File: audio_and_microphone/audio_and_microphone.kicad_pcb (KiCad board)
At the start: 2 copper layers, 61.2 x 60 mm, 30 parts, among them J1 Conn_01x02, J11 Conn_01x02, J2 Conn_01x02, J3 Conn_01x02, J4 Conn_01x02, J5 Conn_01x10_MountingPin, J6 Conn_01x08_MountingPin, J7 Conn_01x08_MountingPin, J8 Conn_01x06_MountingPin, J9 Conn_01x03_Pin

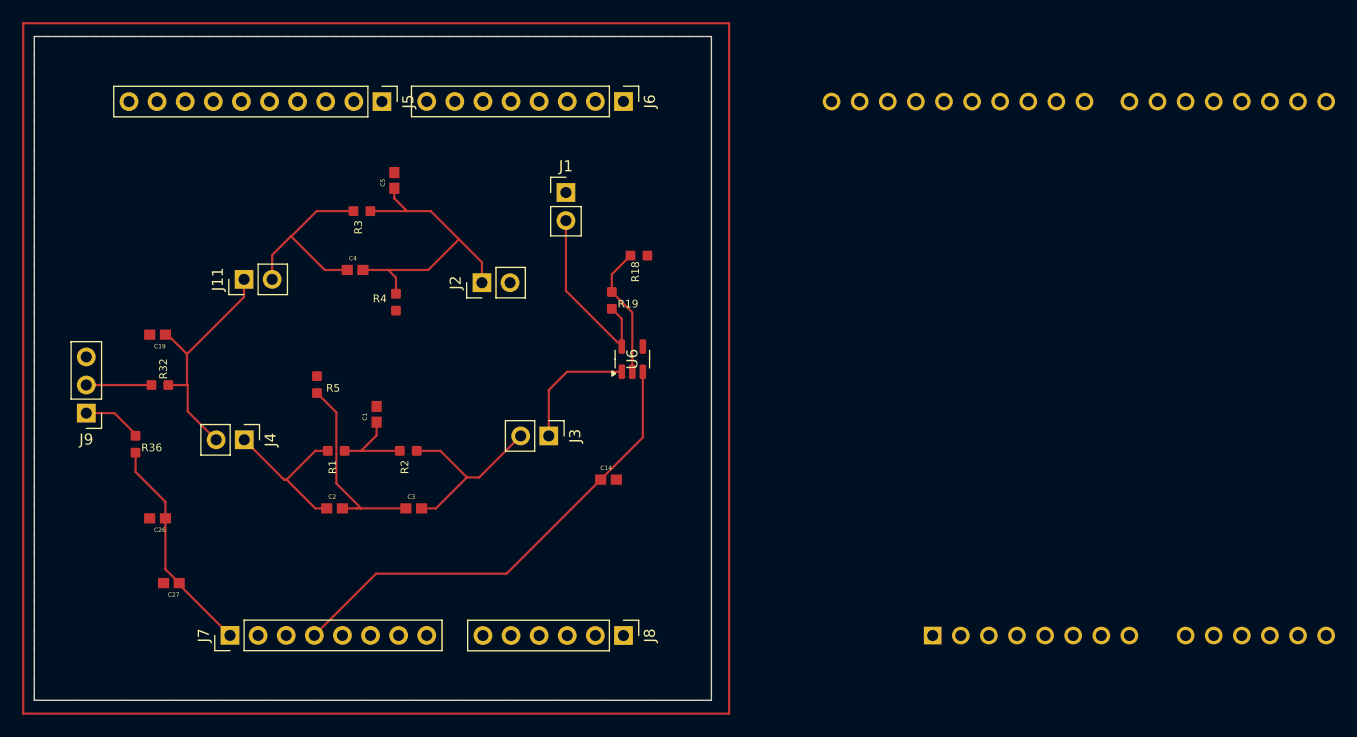
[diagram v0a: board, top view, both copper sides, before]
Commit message: added ground vias to bottom copper layer to fix islands
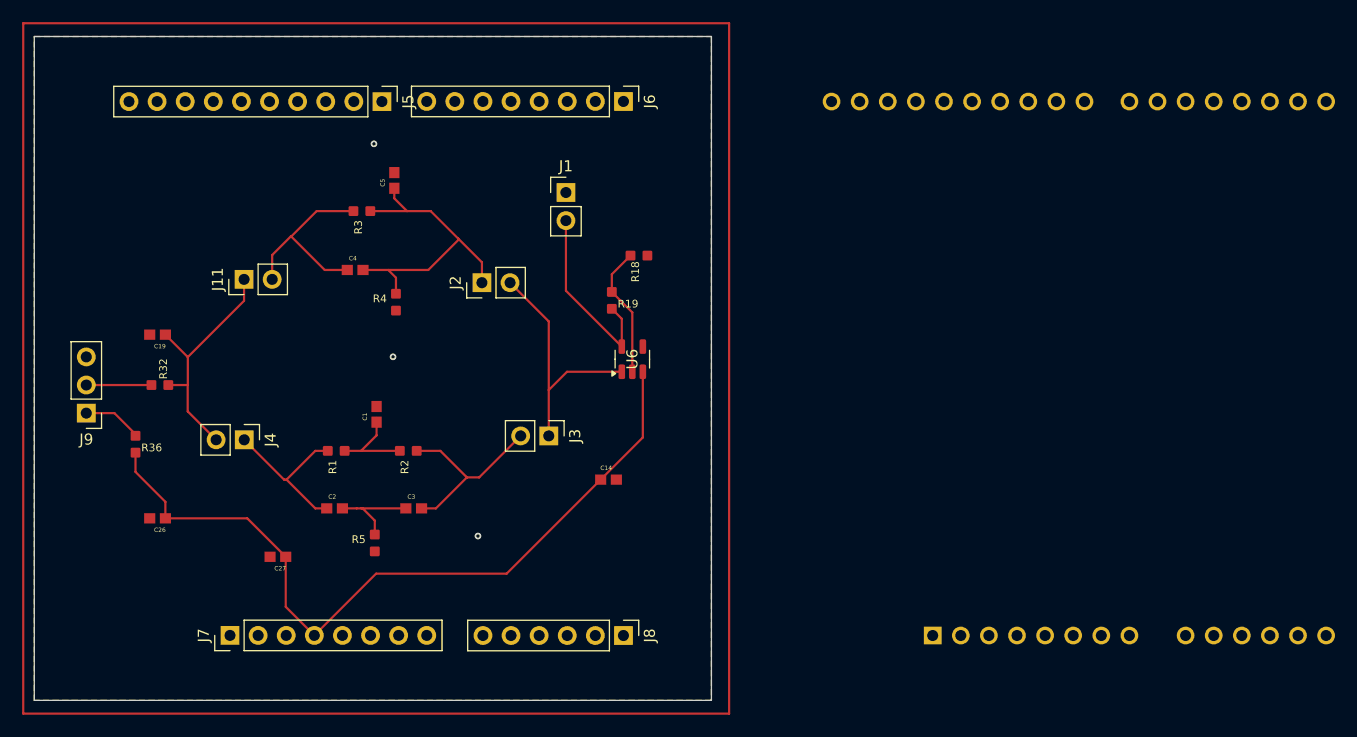
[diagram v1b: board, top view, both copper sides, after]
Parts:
- moved R5 15.2 mm to (66.0, 75.8), turned to 0 degrees
- moved C27 9.91 mm to (57.2, 77.0)
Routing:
- net Net-(J2-Pin_2): track 11.4 -> 22.6 mm
- net Net-(C2-Pad2): track 17.8 -> 8.55 mm
- net +3V3: track 63.1 -> 70.6 mm
- net GND: vias 0 -> 3
- added copper zone on B.Cu, net GND
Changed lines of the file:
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@@
 	(footprint "RC0603FR_072KL:R0603"
 		(layer "F.Cu")
-		(at 60.75 61.462 180)
+		(at 65.975 75.775)
 		(property "Reference" "R5"
 			(at -1.4605 -0.3175 0)
@@
 		)
 		(pad "1" smd roundrect
-			(at 0 -0.762 180)
+			(at 0 -0.762)
 			(size 0.889 0.889)
 			(layers "F.Cu" "F.Mask" "F.Paste")
@@
 		)
 		(pad "2" smd roundrect
-			(at 0 0.762 180)
+			(at 0 0.762)
 			(size 0.889 0.889)
 			(layers "F.Cu" "F.Mask" "F.Paste")
@@
 	(footprint "C1608X5R1E105K080AC:CAPC1608X90N"
 		(layer "F.Cu")
-		(at 47.591 79.4 180)
+		(at 57.216 77.025 180)
 		(property "Reference" "C27"
 			(at -0.21 -1.05 0)
@@
 		(stroke
 			(width 0.2)
-			(type default)
+			(type solid)
 		)
 		(fill no)
 		(layer "F.Cu")
-		(net 61)
 	)
 	(gr_rect
@@
 		(layer "Edge.Cuts")
 	)
+	(via
+		(at 67.625 58.95)
+		(size 0.6)
+		(drill 0.3)
+		(layers "F.Cu" "B.Cu")
+		(free yes)
+		(net 1)
+	)
+	(via
+		(at 75.3 75.15)
+		(size 0.6)
+		(drill 0.3)
+		(layers "F.Cu" "B.Cu")
+		(free yes)
+		(net 1)
+	)
+	(via
+		(at 65.9 39.7)
+		(size 0.6)
+		(drill 0.3)
+		(layers "F.Cu" "B.Cu")
+		(free yes)
+		(net 1)
+	)
 	(segment
 		(start 63.25 67.45)
@@
 	)
 	(segment
-		(start 62.5045 63.9785)
-		(end 60.75 62.224)
+		(start 64.875 72.65)
+		(end 64.75 72.65)
 		(width 0.2)
 		(layer "F.Cu")
@@
 	)
 	(segment
-		(start 64.75 72.65)
-		(end 62.5045 70.4045)
+		(start 68.782 72.65)
+		(end 64.875 72.65)
 		(width 0.2)
 		(layer "F.Cu")
@@
 	)
 	(segment
-		(start 68.782 72.65)
-		(end 64.75 72.65)
+		(start 65.975 75.013)
+		(end 65.975 73.75)
 		(width 0.2)
 		(layer "F.Cu")
@@
 	)
 	(segment
-		(start 62.5045 70.4045)
-		(end 62.5045 63.9785)
+		(start 64.75 72.65)
+		(end 64.335 72.65)
 		(width 0.2)
 		(layer "F.Cu")
@@
 	)
 	(segment
-		(start 64.75 72.65)
-		(end 64.335 72.65)
+		(start 65.975 73.75)
+		(end 64.875 72.65)
 		(width 0.2)
 		(layer "F.Cu")
@@
 	)
 	(segment
-		(start 47.05 78.15)
-		(end 48.3 79.4)
+		(start 60.51 84.13)
+		(end 66.09 78.55)
 		(width 0.2)
 		(layer "F.Cu")
@@
 	)
 	(segment
-		(start 48.3 79.54)
-		(end 52.89 84.13)
+		(start 47.05 73.55)
+		(end 54.45 73.55)
 		(width 0.2)
 		(layer "F.Cu")
@@
 	)
 	(segment
-		(start 48.3 79.4)
-		(end 48.3 79.54)
+		(start 86.391 70.05)
+		(end 90.2 66.241)
 		(width 0.2)
 		(layer "F.Cu")
@@
 	)
 	(segment
-		(start 60.51 84.13)
-		(end 66.09 78.55)
+		(start 57.925 81.545)
+		(end 60.51 84.13)
 		(width 0.2)
 		(layer "F.Cu")
@@
 	)
 	(segment
-		(start 47.05 73.55)
-		(end 47.05 78.15)
+		(start 54.45 73.55)
+		(end 57.925 77.025)
 		(width 0.2)
 		(layer "F.Cu")
@@
 	)
 	(segment
-		(start 86.391 70.05)
-		(end 90.2 66.241)
+		(start 57.925 77.025)
+		(end 57.925 81.545)
 		(width 0.2)
 		(layer "F.Cu")
@@
 	)
 	(segment
-		(start 49 61.435)
-		(end 49 58.7)
+		(start 49.065 63.88)
+		(end 49.065 61.5)
 		(width 0.2)
 		(layer "F.Cu")
@@
 	)
 	(segment
-		(start 54.16 51.95)
-		(end 54.16 53.54)
+		(start 49.075 58.975)
+		(end 54.16 53.89)
 		(width 0.2)
 		(layer "F.Cu")
@@
 	)
 	(segment
-		(start 49.065 63.88)
-		(end 49.065 61.5)
+		(start 47.05 56.95)
+		(end 49.075 58.975)
 		(width 0.2)
 		(layer "F.Cu")
@@
 	)
 	(segment
-		(start 49 58.7)
-		(end 49 58.62)
-		(width 0.2)
-		(layer "F.Cu")
-		(net 72)
-	)
-	(segment
-		(start 49.065 61.5)
-		(end 49 61.435)
+		(start 49.075 61.49)
+		(end 49.065 61.5)
 		(width 0.2)
 		(layer "F.Cu")
@@
 	)
 	(segment
-		(start 47.25 56.95)
-		(end 47.05 56.95)
+		(start 49.075 58.975)
+		(end 49.075 61.49)
 		(width 0.2)
 		(layer "F.Cu")
@@
 	)
 	(segment
-		(start 54.16 53.54)
-		(end 49 58.7)
+		(start 54.16 53.89)
+		(end 54.16 51.95)
 		(width 0.2)
 		(layer "F.Cu")
@@
 	)
 	(segment
-		(start 49 58.7)
-		(end 47.25 56.95)
+		(start 81.7 55.75)
+		(end 81.7 61.95)
 		(width 0.2)
 		(layer "F.Cu")
-		(net 72)
+		(net 73)
 	)
 	(segment
@@
 		(net 73)
 	)
+	(segment
+		(start 78.2 52.25)
+		(end 81.7 55.75)
+		(width 0.2)
+		(layer "F.Cu")
+		(net 73)
+	)
 	(zone
 		(net 1)
 		(net_name "GND")
-		(layer "F.Cu")
+		(layers "F.Cu" "B.Cu")
 		(hatch edge 0.5)
 		(priority 1)

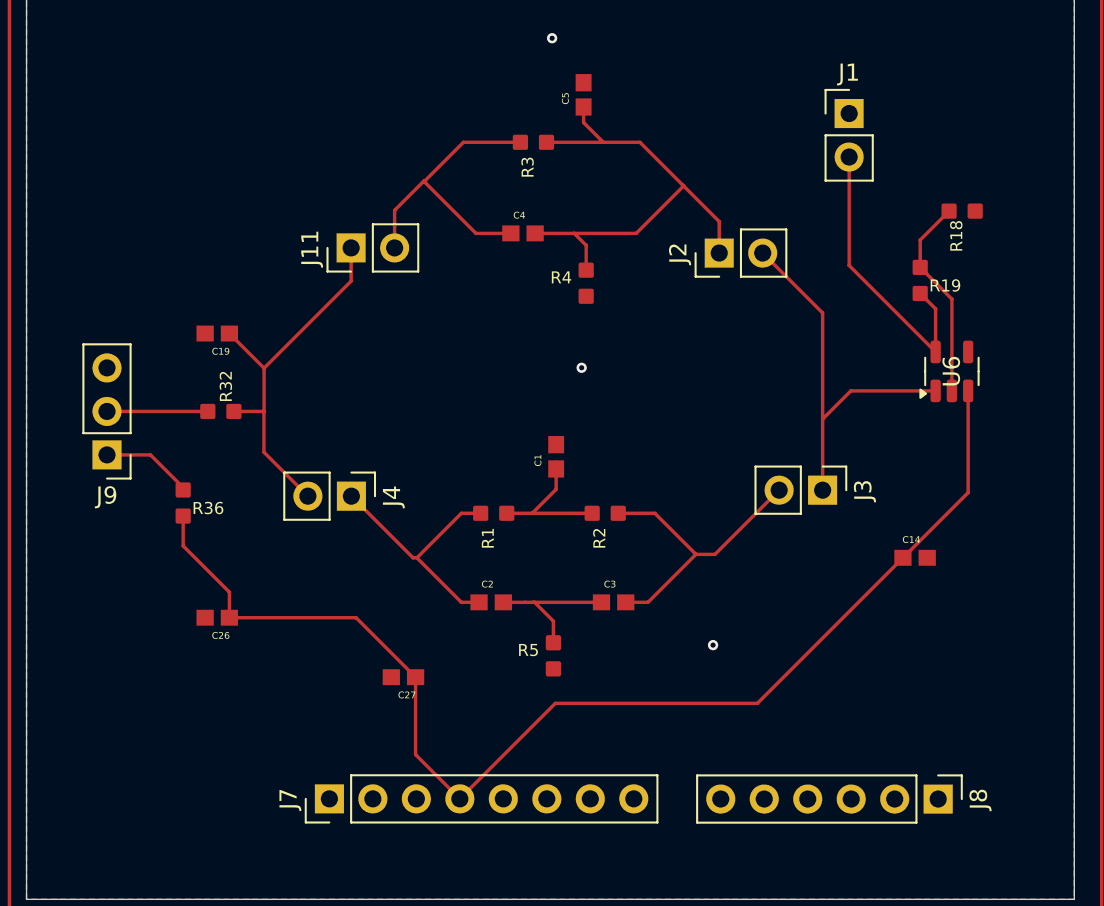
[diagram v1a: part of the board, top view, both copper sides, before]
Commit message: labeled schematic and fixed track widths in pcb. passed drc
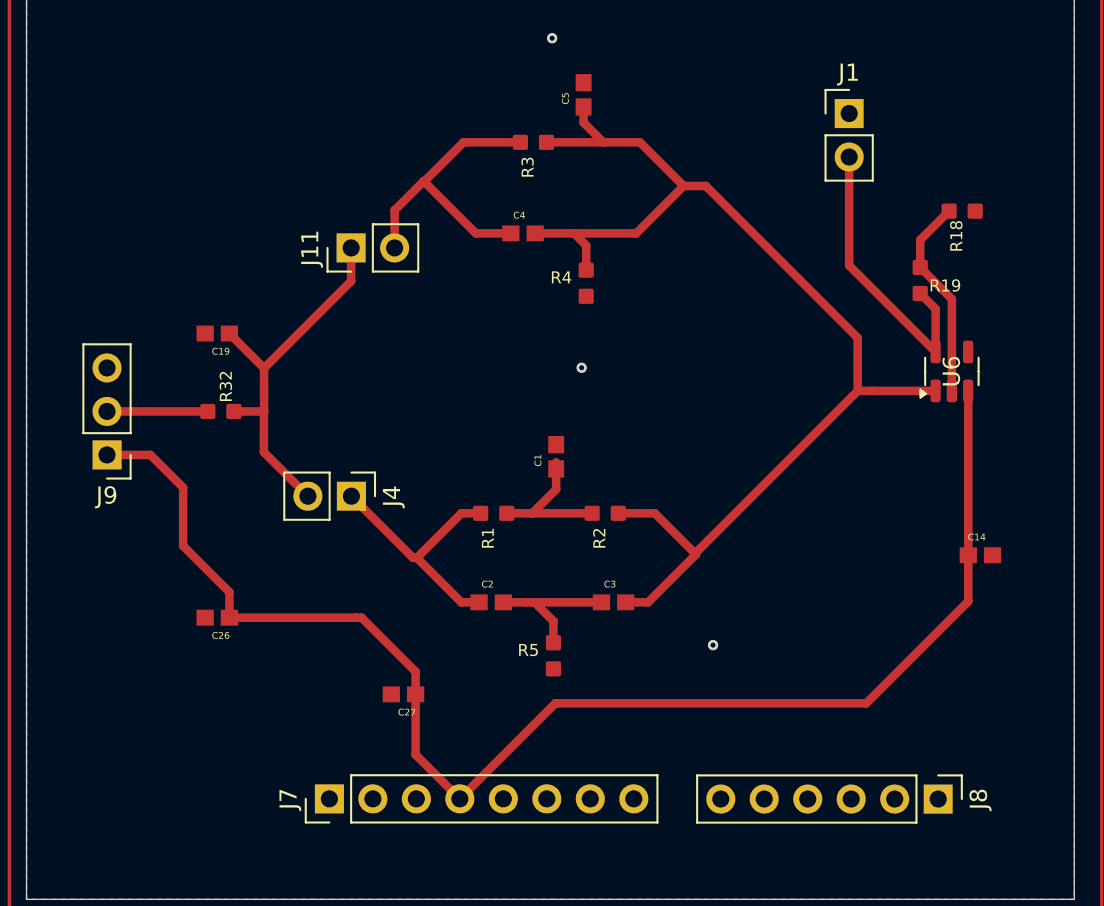
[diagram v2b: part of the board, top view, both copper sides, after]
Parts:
- removed J2, J3: Conn_01x02, Connector_PinHeader_2.54mm:PinHeader_1x02_P2.54mm_Vertical
- removed R36: 0, RC0603FR_072KL:R0603
- moved C14 3.82 mm to (90.9, 69.9)
- moved C27 1.00 mm to (57.2, 78.0)
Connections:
- net Net-(J11-Pin_1) renamed /low_pass_filter
- C3 pad 2: Net-(J3-Pin_2) -> /new_notch
- C4 pad 2: Net-(J2-Pin_1) -> /new_notch
- C5 pad 1: Net-(J2-Pin_1) -> /new_notch
- J7 pad 1: +3V3 -> (no net)
- J7 pad 2: +3V3 -> (no net)
- J9 pad 1: Net-(J9-Pin_1) -> +3V3
- R2 pad 2: Net-(J3-Pin_2) -> /new_notch
- R3 pad 2: Net-(J2-Pin_1) -> /new_notch
- R4 pad 1: Net-(J2-Pin_1) -> /new_notch
- U6 pad 1: Net-(J2-Pin_2) -> /new_notch
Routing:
- net /new_notch: track 0.00 -> 69.6 mm
- net Net-(J2-Pin_1): track 28.6 -> 0.00 mm
- net Net-(J2-Pin_2): track 22.6 -> 0.00 mm
- net Net-(J3-Pin_2): track 17.2 -> 0.00 mm
- net +3V3: track 70.6 -> 81.4 mm
- net Net-(J9-Pin_1): track 5.38 -> 0.00 mm

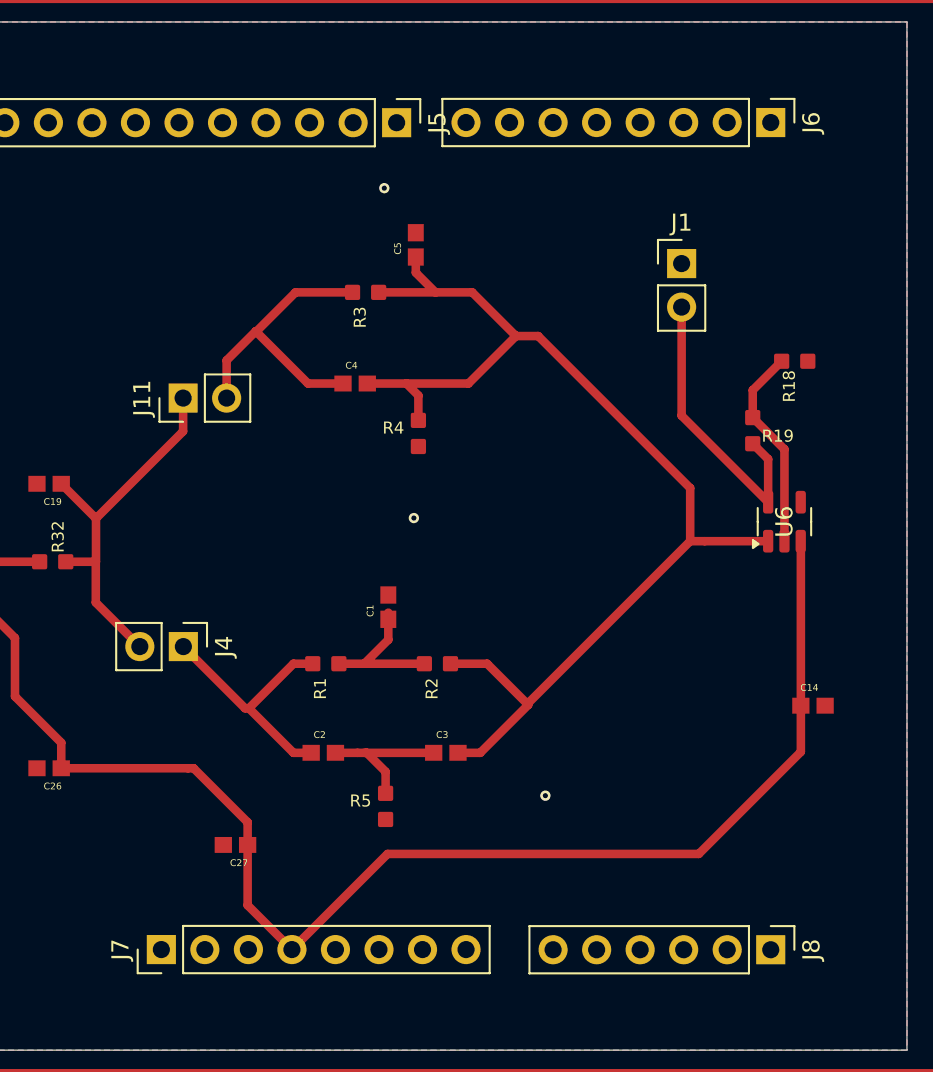
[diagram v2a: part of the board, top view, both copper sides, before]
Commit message: added labels on pcb
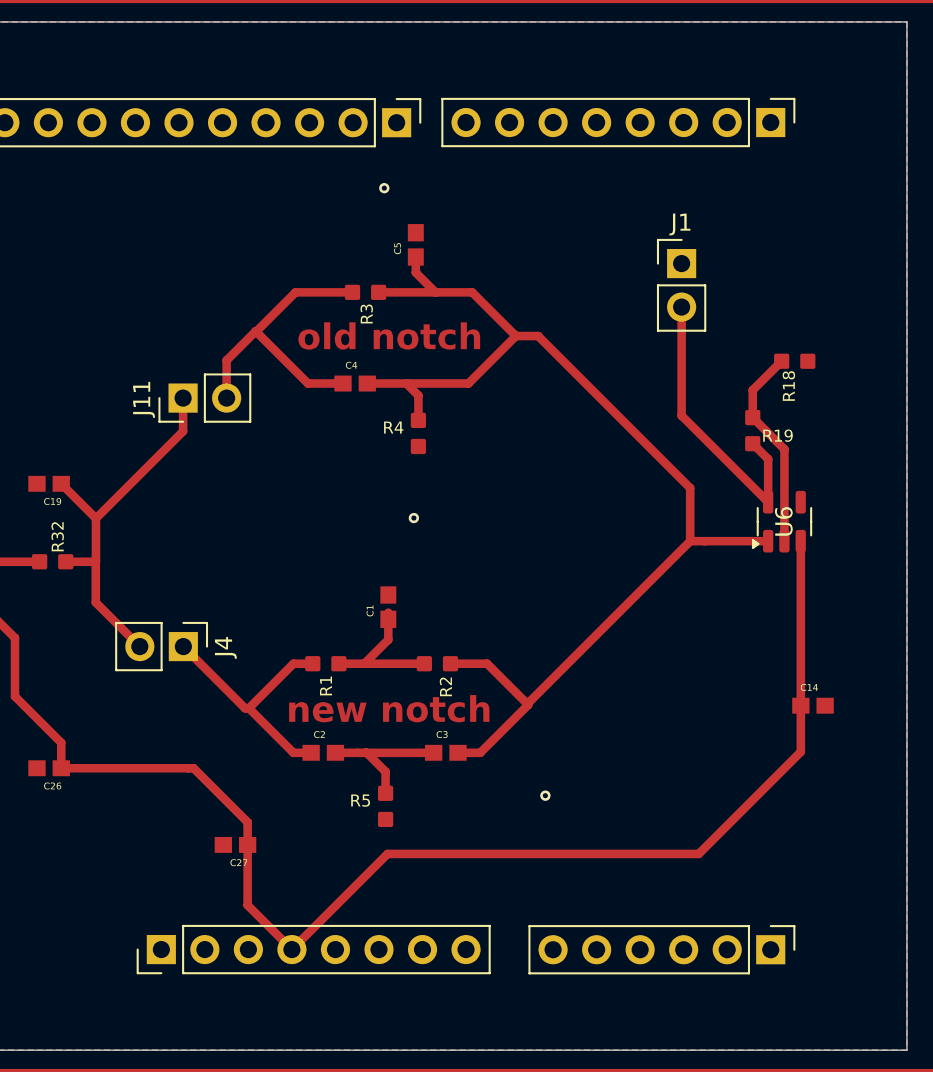
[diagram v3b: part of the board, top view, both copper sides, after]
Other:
- board text added: "new notch"
- board text added: "old notch"
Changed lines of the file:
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@@
 		(at 62.488 67.45 90)
 		(property "Reference" "R1"
-			(at -1.4605 -0.3175 90)
+			(at -1.3 0.037 90)
 			(layer "F.SilkS")
 			(effects
@@
 			(at 0 -2.38 90)
 			(layer "F.SilkS")
+			(hide yes)
 			(effects
 				(font
@@
 			(at 0 -2.38 90)
 			(layer "F.SilkS")
+			(hide yes)
 			(effects
 				(font
@@
 			(at 0 -2.38 90)
 			(layer "F.SilkS")
+			(hide yes)
 			(effects
 				(font
@@
 		(at 69 67.45 90)
 		(property "Reference" "R2"
-			(at -1.4605 -0.3175 90)
+			(at -1.35 0.525 90)
 			(layer "F.SilkS")
 			(effects
@@
 		(at 64.8095 45.78 90)
 		(property "Reference" "R3"
-			(at -1.4605 -0.3175 90)
+			(at -1.27 0.0905 90)
 			(layer "F.SilkS")
 			(effects
@@
 			(at 0 -2.38 90)
 			(layer "F.SilkS")
+			(hide yes)
 			(effects
 				(font
@@
 		(layer "Edge.Cuts")
 	)
+	(gr_text "new notch"
+		(at 60.175 71.025 0)
+		(layer "F.Cu")
+		(effects
+			(font
+				(size 1.5 1.5)
+				(thickness 0.3)
+				(bold yes)
+			)
+			(justify left bottom)
+		)
+	)
+	(gr_text "old notch"
+		(at 60.8 49.275 0)
+		(layer "F.Cu")
+		(effects
+			(font
+				(size 1.5 1.5)
+				(thickness 0.3)
+				(bold yes)
+			)
+			(justify left bottom)
+		)
+	)
 	(via
